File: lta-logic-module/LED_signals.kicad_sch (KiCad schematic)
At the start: 21 parts

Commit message: Fix GND path return.
* Route power traces over ground plane.
* Add routed corners to edge cuts
* Remove final TODO notes.
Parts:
- J3, J4: Comment (none) -> Molex Micro-Latch 12-pin
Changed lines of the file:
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@@
       (effects (font (size 1.524 1.524)) hide)
     )
-    (property "Comment" "" (id 4) (at 264.795 24.765 0)
+    (property "Comment" "Molex Micro-Latch 12-pin" (id 4) (at 264.795 24.765 0)
       (effects (font (size 1.27 1.27)) hide)
     )
@@
       (effects (font (size 1.524 1.524)) hide)
     )
-    (property "Comment" "" (id 4) (at 264.795 66.04 0)
-      (effects (font (size 1.27 1.27)) hide)
-    )
+    (property "Comment" "Molex Micro-Latch 12-pin" (id 4) (at 264.795 66.04 0)
+      (effects (font (size 1.27 1.27)) hide)
+    )

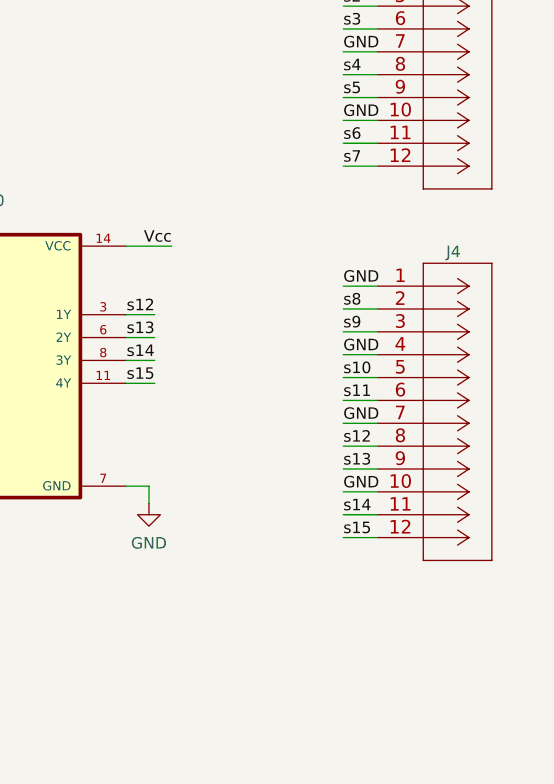
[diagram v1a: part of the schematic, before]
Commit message: Add indicator LED to SW1 enabled.
Adds 220K pull-down resistor to DARK signal. (Validated.)
Update solder thief pads and process direction indicator.
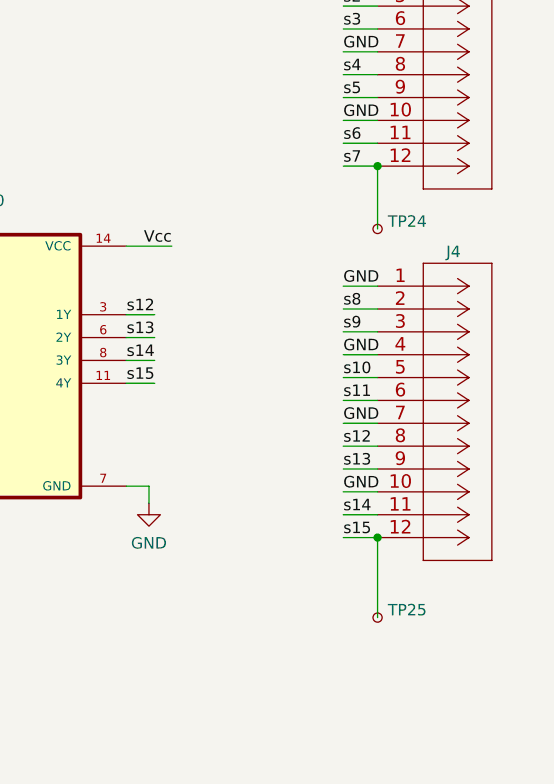
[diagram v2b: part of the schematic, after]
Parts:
- added TP24, TP25: (no value), symbol Connector:TestPoint_Small
- J3, J4: Comment Molex Micro-Latch 12-pin -> Molex Micro-Latch, 12-pin
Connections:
- net s15: now also TP25.1
- net s7: now also TP24.1
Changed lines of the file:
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@@
   (junction (at 28.575 184.785) (diameter 0) (color 0 0 0 0)
   )
+  (junction (at 264.795 93.98) (diameter 0) (color 0 0 0 0)
+  )
   (junction (at 99.06 123.19) (diameter 0) (color 0 0 0 0)
   )
@@
   )
   (junction (at 90.17 115.57) (diameter 0) (color 0 0 0 0)
+  )
+  (junction (at 264.795 52.705) (diameter 0) (color 0 0 0 0)
   )
   (junction (at 130.81 154.305) (diameter 0) (color 0 0 0 0)
@@
     (stroke (width 0) (type default) (color 0 0 0 0))
   )
+  (wire (pts (xy 264.795 93.98) (xy 264.795 102.87))
+    (stroke (width 0) (type default) (color 0 0 0 0))
+  )
   (wire (pts (xy 128.27 151.765) (xy 128.27 154.305))
     (stroke (width 0) (type default) (color 0 0 0 0))
@@
   )
   (wire (pts (xy 142.24 88.265) (xy 142.24 90.17))
+    (stroke (width 0) (type default) (color 0 0 0 0))
+  )
+  (wire (pts (xy 264.795 52.705) (xy 264.795 59.69))
     (stroke (width 0) (type default) (color 0 0 0 0))
   )
@@
     )
     (property "Datasheet" "" (id 3) (at 191.135 90.17 0)
+      (effects (font (size 1.27 1.27)) hide)
+    )
+    (pin "1")
+  )
+  (symbol (lib_id "Connector:TestPoint_Small") (at 264.795 59.69 0) (unit 1)
+    (in_bom no) (on_board yes)
+    (property "Reference" "TP24" (id 0) (at 265.938 58.8553 0)
+      (effects (font (size 1.27 1.27)) (justify left))
+    )
+    (property "Value" "" (id 1) (at 265.938 61.3922 0)
+      (effects (font (size 1.27 1.27)) (justify left))
+    )
+    (property "Footprint" "" (id 2) (at 269.875 59.69 0)
+      (effects (font (size 1.27 1.27)) hide)
+    )
+    (property "Datasheet" "~" (id 3) (at 269.875 59.69 0)
       (effects (font (size 1.27 1.27)) hide)
     )
@@
       (effects (font (size 1.524 1.524)) hide)
     )
-    (property "Comment" "Molex Micro-Latch 12-pin" (id 4) (at 264.795 24.765 0)
+    (property "Comment" "Molex Micro-Latch, 12-pin" (id 4) (at 264.795 24.765 0)
       (effects (font (size 1.27 1.27)) hide)
     )
@@
     (pin "1")
     (pin "2")
+  )
+  (symbol (lib_id "Connector:TestPoint_Small") (at 264.795 102.87 0) (unit 1)
+    (in_bom no) (on_board yes)
+    (property "Reference" "TP25" (id 0) (at 265.938 102.0353 0)
+      (effects (font (size 1.27 1.27)) (justify left))
+    )
+    (property "Value" "" (id 1) (at 265.938 104.5722 0)
+      (effects (font (size 1.27 1.27)) (justify left))
+    )
+    (property "Footprint" "" (id 2) (at 269.875 102.87 0)
+      (effects (font (size 1.27 1.27)) hide)
+    )
+    (property "Datasheet" "~" (id 3) (at 269.875 102.87 0)
+      (effects (font (size 1.27 1.27)) hide)
+    )
+    (pin "1")
   )
   (symbol (lib_id "Aaron-TI-74xx:SN74LVC00AD") (at 224.155 78.105 0) (unit 1)
@@
       (effects (font (size 1.524 1.524)) hide)
     )
-    (property "Comment" "Molex Micro-Latch 12-pin" (id 4) (at 264.795 66.04 0)
-      (effects (font (size 1.27 1.27)) hide)
-    )
+    (property "Comment" "Molex Micro-Latch, 12-pin" (id 4) (at 264.795 66.04 0)
+      (effects (font (size 1.27 1.27)) hide)
+    )

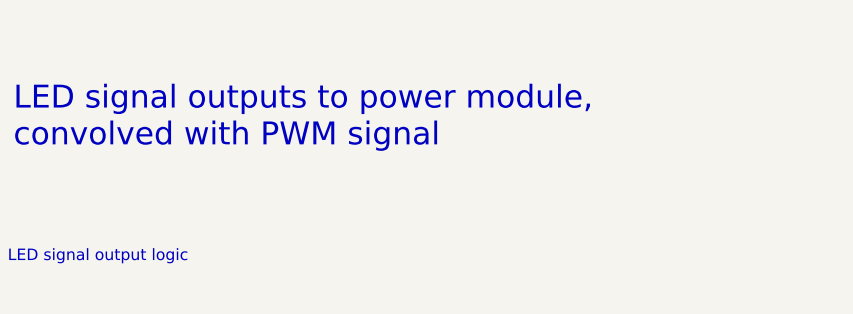
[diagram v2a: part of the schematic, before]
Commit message: Generate logic module 2022-05-08 v1.0 fab documentation.
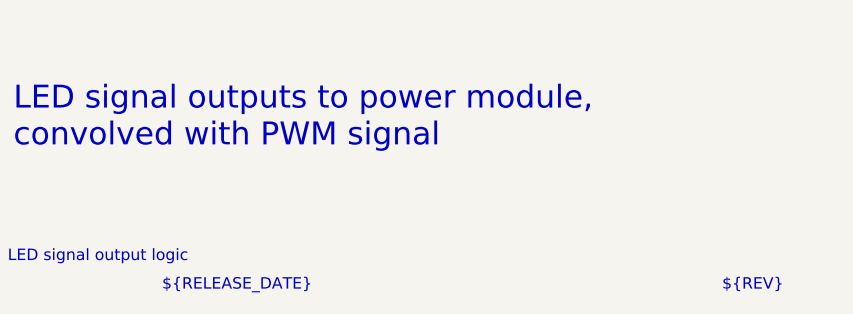
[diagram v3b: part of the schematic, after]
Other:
- note added: "${RELEASE_DATE}"
- note added: "${REV}"
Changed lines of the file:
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@@
     (stroke (width 0) (type default) (color 0 0 0 0))
+  )
+  (text "${RELEASE_DATE}" (at 207.645 193.675 0)
+    (effects (font (size 1.27 1.27)) (justify left bottom))
   )
   (text "Connector to power module" (at 250.8001 17.7314 0)
@@
     (effects (font (size 1.27 1.27)) (justify left bottom))
   )
+  (text "${REV}" (at 269.875 193.675 0)
+    (effects (font (size 1.27 1.27)) (justify left bottom))
+  )

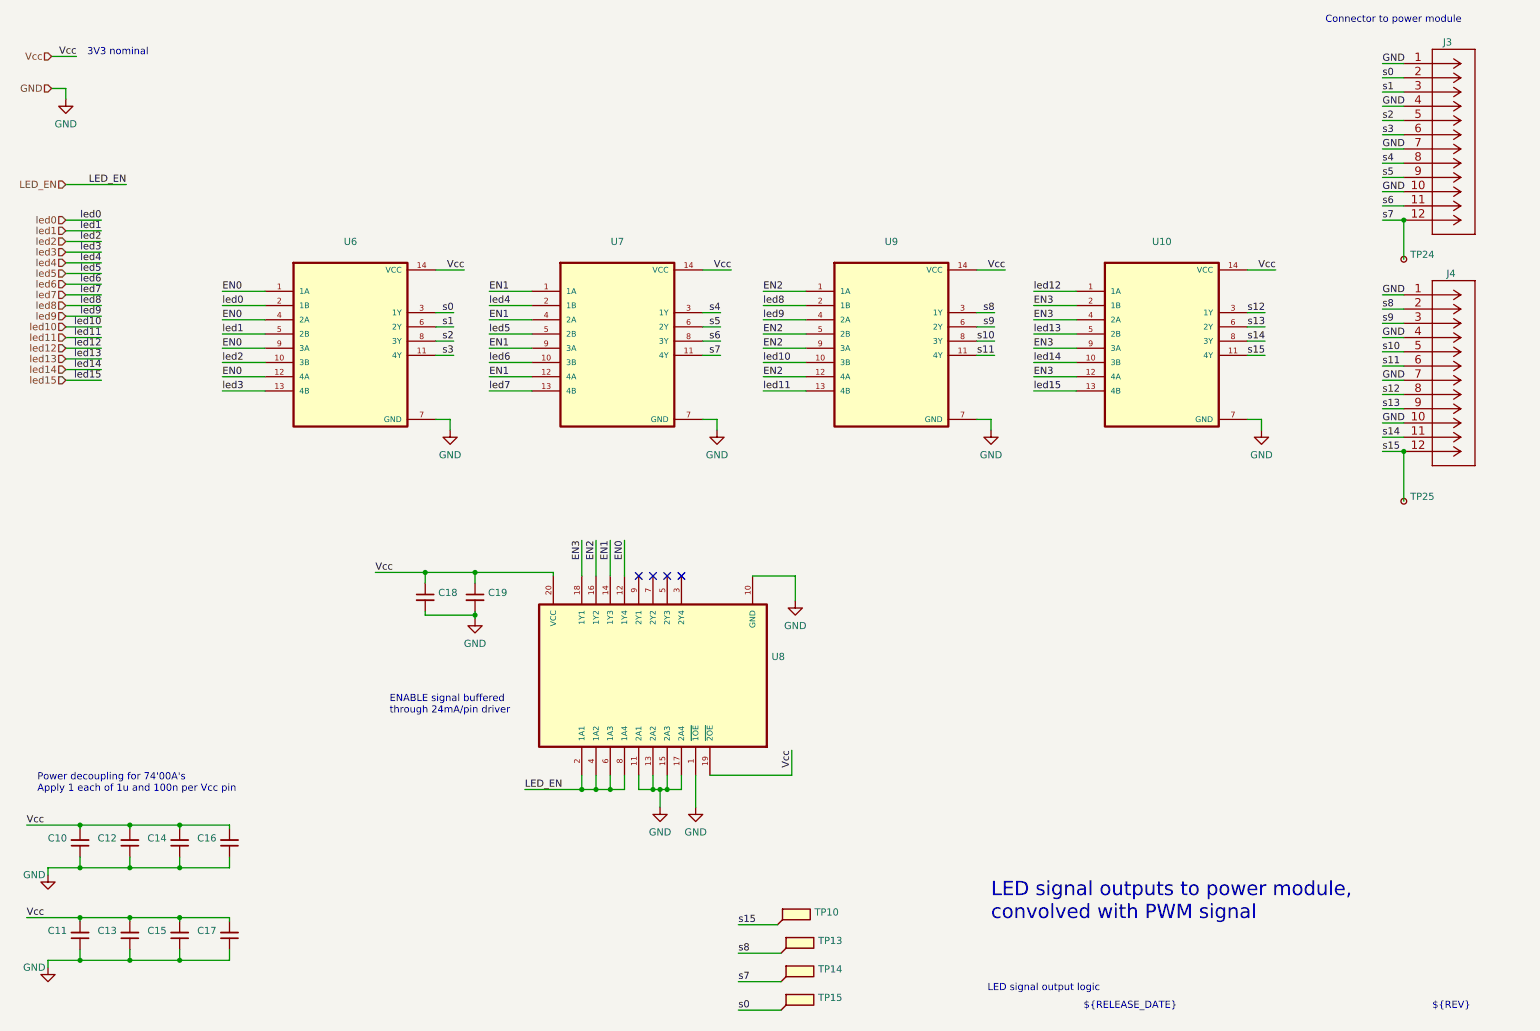
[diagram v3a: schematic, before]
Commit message: Update logic module power budget from button LED measurements.
Button LEDs draw ~11mA each (98 mA total) empirically; not the ~20mA each
I initially guessed for estimating purposes.
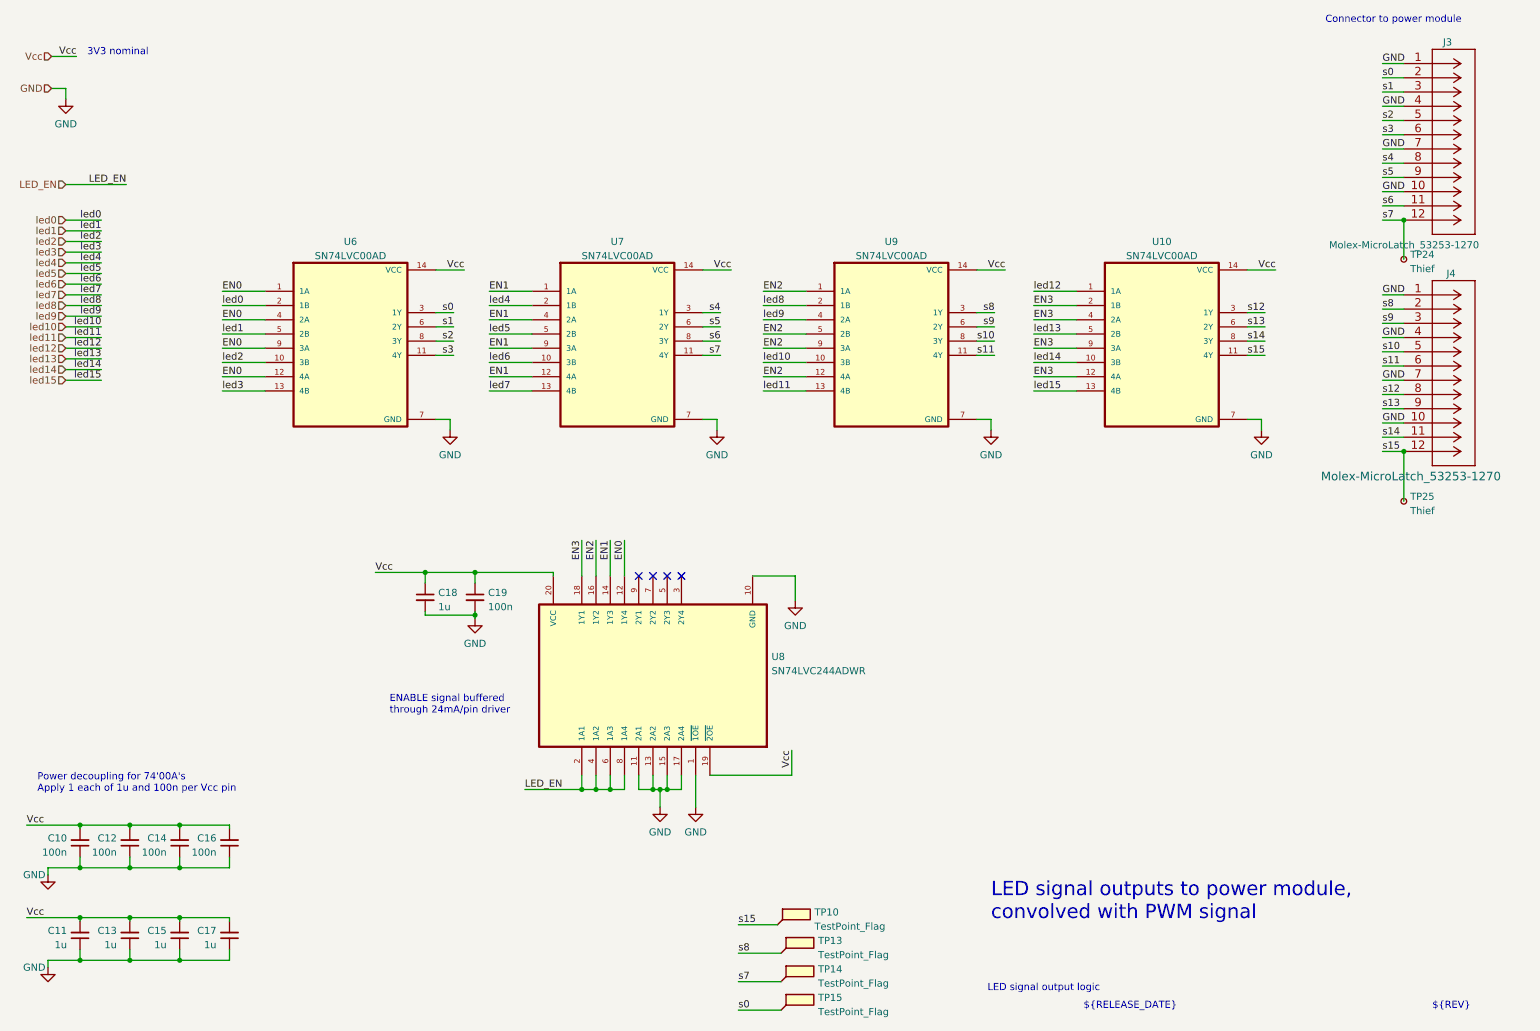
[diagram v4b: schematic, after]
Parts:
- C10, C12, C14, C16, C19: value (none) -> 100n; footprint (none) -> Capacitor_SMD:C_0603_1608Metric
- C11, C13, C15, C17, C18: value (none) -> 1u; footprint (none) -> Capacitor_SMD:C_0603_1608Metric
- J3, J4: value (none) -> Molex-MicroLatch_53253-1270; footprint (none) -> Aaron_THT:Molex-MicroLatch-53253-1270
- TP10, TP13, TP14, TP15: value (none) -> TestPoint_Flag; footprint (none) -> Aaron_THT:TestPoint_THTPad_1.0x1.0mm_Drill0.3mm
- TP24, TP25: value (none) -> Thief; footprint (none) -> Aaron_Pads:Pad_D1.0mm
- U10, U6, U7, U9: value (none) -> SN74LVC00AD; footprint (none) -> Aaron_TI_Parts:TI_SOIC_D_R-PDSO-G14
- U8: value (none) -> SN74LVC244ADWR; footprint (none) -> Aaron_TI_Parts:TI_SOIC_DW0020A
